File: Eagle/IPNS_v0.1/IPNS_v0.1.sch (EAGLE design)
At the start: 30 parts, among them Q1 16MHz, Q2 32.768 kHz, U1 STM8L152C4_C6TX

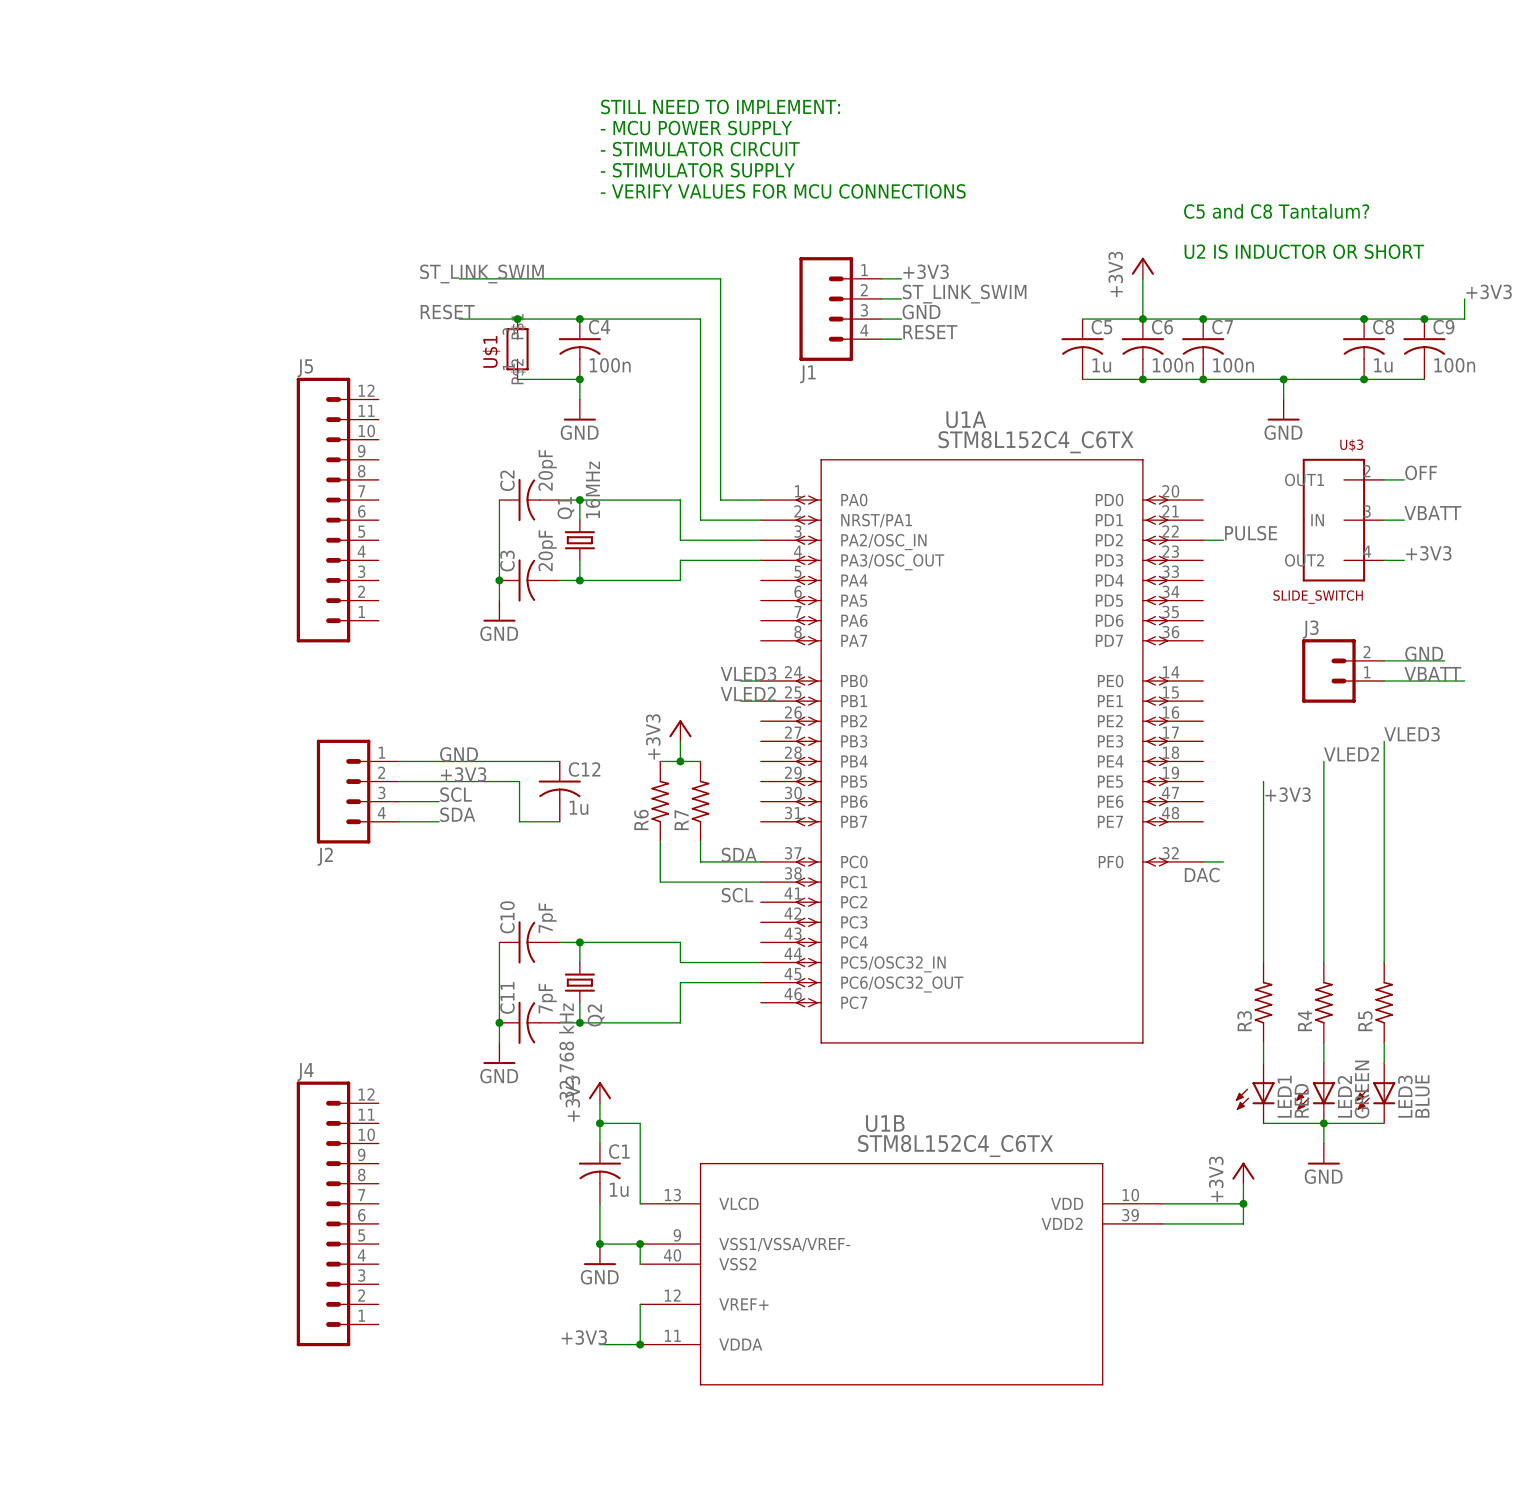
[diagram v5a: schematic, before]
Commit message: Routed Vbatt, Vmcu (3.3V), GND, and PWM and DAC to breakout pins
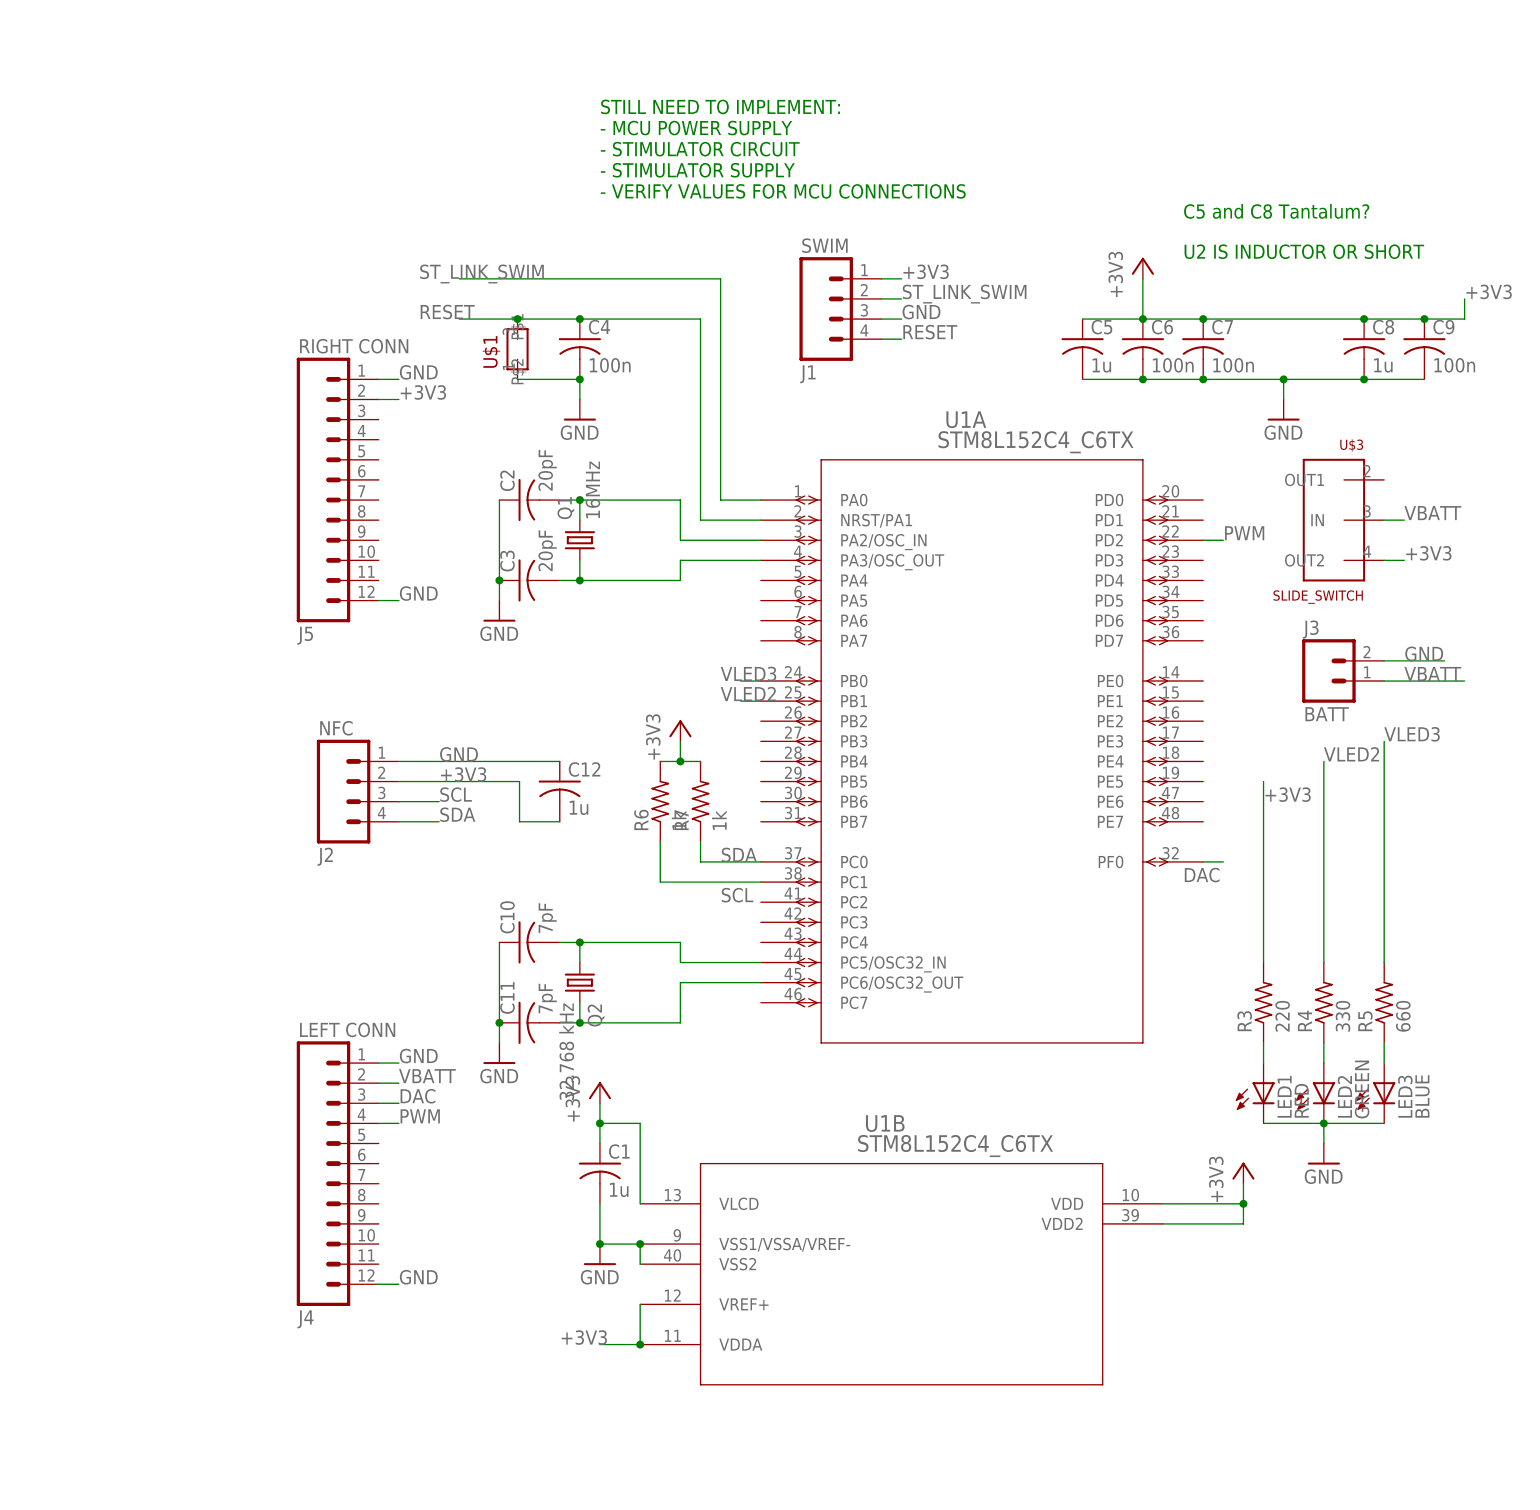
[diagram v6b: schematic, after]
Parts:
- J1: value (none) -> SWIM
- J2: value (none) -> NFC
- J3: value (none) -> BATT
- J4: value (none) -> LEFT CONN
- J5: value (none) -> RIGHT CONN
- R3: value (none) -> 220
- R4: value (none) -> 330
- R5: value (none) -> 660
- R6, R7: value (none) -> 1k
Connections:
- removed net OFF: U$3.OUT1
- removed net PULSE: U1A.PD2
- new net PWM: J4.4, U1A.PD2
- net +3V3: now also J5.2
- net DAC: now also J4.3
- net GND: now also J4.1, J4.12, J5.1, J5.12
- net VBATT: now also J4.2
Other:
- moved on the sheet: J4, J5
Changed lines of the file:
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@@
 <part name="C3" library="IPNS_Lib_v0.1" deviceset="C-US" device="C0805" value="20pF"/>
 <part name="GND2" library="IPNS_Lib_v0.1" deviceset="GND" device=""/>
-<part name="J1" library="IPNS_Lib_v0.1" deviceset="M04" device="PTH"/>
+<part name="J1" library="IPNS_Lib_v0.1" deviceset="M04" device="PTH" value="SWIM"/>
 <part name="U$1" library="IPNS_Lib_v0.1" deviceset="PUSH-BUTTON" device=""/>
 <part name="C4" library="IPNS_Lib_v0.1" deviceset="C-US" device="C0805" value="100n"/>
@@
 <part name="C11" library="IPNS_Lib_v0.1" deviceset="C-US" device="C0805" value="7pF"/>
 <part name="GND5" library="IPNS_Lib_v0.1" deviceset="GND" device=""/>
-<part name="R3" library="IPNS_Lib_v0.1" deviceset="R-US_" device="R0805"/>
-<part name="R4" library="IPNS_Lib_v0.1" deviceset="R-US_" device="R0805"/>
-<part name="R5" library="IPNS_Lib_v0.1" deviceset="R-US_" device="R0805"/>
+<part name="R3" library="IPNS_Lib_v0.1" deviceset="R-US_" device="R0805" value="220"/>
+<part name="R4" library="IPNS_Lib_v0.1" deviceset="R-US_" device="R0805" value="330"/>
+<part name="R5" library="IPNS_Lib_v0.1" deviceset="R-US_" device="R0805" value="660"/>
 <part name="LED1" library="led" deviceset="LED" device="CHIP-LED0805" value="RED"/>
 <part name="LED2" library="led" deviceset="LED" device="CHIP-LED0805" value="GREEN"/>
 <part name="LED3" library="led" deviceset="LED" device="CHIP-LED0805" value="BLUE"/>
 <part name="GND6" library="IPNS_Lib_v0.1" deviceset="GND" device=""/>
-<part name="J2" library="IPNS_Lib_v0.1" deviceset="M04" device="PTH"/>
+<part name="J2" library="IPNS_Lib_v0.1" deviceset="M04" device="PTH" value="NFC"/>
 <part name="C12" library="IPNS_Lib_v0.1" deviceset="C-US" device="C0805" value="1u"/>
-<part name="R6" library="IPNS_Lib_v0.1" deviceset="R-US_" device="R0805"/>
-<part name="R7" library="IPNS_Lib_v0.1" deviceset="R-US_" device="R0805"/>
+<part name="R6" library="IPNS_Lib_v0.1" deviceset="R-US_" device="R0805" value="1k"/>
+<part name="R7" library="IPNS_Lib_v0.1" deviceset="R-US_" device="R0805" value="1k"/>
 <part name="+3V4" library="IPNS_Lib_v0.1" deviceset="+3V3" device=""/>
 <part name="U$3" library="IPNS_Lib_v0.1" deviceset="SLIDE_SWITCH" device=""/>
-<part name="J3" library="IPNS_Lib_v0.1" deviceset="M02" device="PTH"/>
-<part name="J4" library="IPNS_Lib_v0.1" deviceset="M12" device="PTH"/>
-<part name="J5" library="IPNS_Lib_v0.1" deviceset="M12" device="PTH"/>
+<part name="J3" library="IPNS_Lib_v0.1" deviceset="M02" device="PTH" value="BATT"/>
+<part name="J4" library="IPNS_Lib_v0.1" deviceset="M12" device="PTH" value="LEFT CONN"/>
+<part name="J5" library="IPNS_Lib_v0.1" deviceset="M12" device="PTH" value="RIGHT CONN"/>
 </parts>
 <sheets>
@@
 <instance part="U$3" gate="G$1" x="83.82" y="91.44" rot="MR0"/>
 <instance part="J3" gate="G$1" x="83.82" y="71.12"/>
-<instance part="J4" gate="G$1" x="-45.72" y="5.08"/>
-<instance part="J5" gate="G$1" x="-45.72" y="93.98"/>
+<instance part="J4" gate="G$1" x="-45.72" y="7.62" rot="MR180"/>
+<instance part="J5" gate="G$1" x="-45.72" y="93.98" rot="MR180"/>
 </instances>
 <busses>
@@
 <label x="76.2" y="55.88" size="1.778" layer="95"/>
 </segment>
+<segment>
+<pinref part="J5" gate="G$1" pin="2"/>
+<wire x1="-35.56" y1="106.68" x2="-33.02" y2="106.68" width="0.1524" layer="91"/>
+<label x="-33.02" y="106.68" size="1.778" layer="95"/>
+</segment>
 </net>
 <net name="GND" class="0">
@@
 <label x="93.98" y="73.66" size="1.778" layer="95"/>
 </segment>
+<segment>
+<pinref part="J5" gate="G$1" pin="12"/>
+<wire x1="-35.56" y1="81.28" x2="-33.02" y2="81.28" width="0.1524" layer="91"/>
+<label x="-33.02" y="81.28" size="1.778" layer="95"/>
+</segment>
+<segment>
+<pinref part="J4" gate="G$1" pin="12"/>
+<wire x1="-35.56" y1="-5.08" x2="-33.02" y2="-5.08" width="0.1524" layer="91"/>
+<label x="-33.02" y="-5.08" size="1.778" layer="95"/>
+</segment>
+<segment>
+<pinref part="J5" gate="G$1" pin="1"/>
+<wire x1="-35.56" y1="109.22" x2="-33.02" y2="109.22" width="0.1524" layer="91"/>
+<label x="-33.02" y="109.22" size="1.778" layer="95"/>
+</segment>
+<segment>
+<pinref part="J4" gate="G$1" pin="1"/>
+<wire x1="-35.56" y1="22.86" x2="-33.02" y2="22.86" width="0.1524" layer="91"/>
+<label x="-33.02" y="22.86" size="1.778" layer="95"/>
+</segment>
 </net>
 <net name="N$1" class="0">
@@
 <label x="66.04" y="45.72" size="1.778" layer="95"/>
 </segment>
-</net>
-<net name="PULSE" class="0">
-<segment>
-<pinref part="U1" gate="A" pin="PD2"/>
-<wire x1="68.58" y1="88.9" x2="71.12" y2="88.9" width="0.1524" layer="91"/>
-<label x="71.12" y="88.9" size="1.778" layer="95"/>
+<segment>
+<pinref part="J4" gate="G$1" pin="3"/>
+<wire x1="-35.56" y1="17.78" x2="-33.02" y2="17.78" width="0.1524" layer="91"/>
+<label x="-33.02" y="17.78" size="1.778" layer="95"/>
 </segment>
 </net>
@@
 <label x="93.98" y="71.12" size="1.778" layer="95"/>
 </segment>
-</net>
-<net name="OFF" class="0">
-<segment>
-<pinref part="U$3" gate="G$1" pin="OUT1"/>
-<wire x1="91.44" y1="96.52" x2="93.98" y2="96.52" width="0.1524" layer="91"/>
-<label x="93.98" y="96.52" size="1.778" layer="95"/>
+<segment>
+<pinref part="J4" gate="G$1" pin="2"/>
+<wire x1="-35.56" y1="20.32" x2="-33.02" y2="20.32" width="0.1524" layer="91"/>
+<label x="-33.02" y="20.32" size="1.778" layer="95"/>
+</segment>
+</net>
+<net name="PWM" class="0">
+<segment>
+<pinref part="J4" gate="G$1" pin="4"/>
+<wire x1="-35.56" y1="15.24" x2="-33.02" y2="15.24" width="0.1524" layer="91"/>
+<label x="-33.02" y="15.24" size="1.778" layer="95"/>
+</segment>
+<segment>
+<pinref part="U1" gate="A" pin="PD2"/>
+<wire x1="68.58" y1="88.9" x2="71.12" y2="88.9" width="0.1524" layer="91"/>
+<label x="71.12" y="88.9" size="1.778" layer="95"/>
 </segment>
 </net>
@@
 </sheet>
 </sheets>
+<errors>
+</errors>
 </schematic>
 </drawing>
